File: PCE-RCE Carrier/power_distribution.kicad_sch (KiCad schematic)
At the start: 21 parts, among them J2 XT60PW-F, J3 XT60PW-F, J4 XT60PW-F, J8 Conn_01x02_Pin, U1 TPS75533KTTRG3, U2 TPS54302DDCR, U3 BD6222HFP-TR

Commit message: stoning my cap
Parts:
- removed CR1: SDM40E20LC-7, SOT-23_DIO, symbol SDM40E20LC_7:SDM40E20LC-7
- added D1: RB496EATR, DIO_FTZ_ROM, symbol RB496EATR:RB496EATR
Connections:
- net VBAT1: now also D1.1
- net VBAT2: now also D1.3
- net at J4.1: now also D1.4, D1.5
- no-connect marks 1 -> 2
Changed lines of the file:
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@@
+	)
+	(junction
+		(at 86.36 81.28)
+		(diameter 0)
+		(color 0 0 0 0)
 	)
 	(junction
@@
 	)
 	(no_connect
+		(at 55.88 86.36)
+	)
+	(no_connect
 		(at 93.98 88.9)
 	)
@@
 	(wire
 		(pts
+			(xy 52.07 91.44) (xy 55.88 91.44)
+		)
+		(stroke
+			(width 0)
+			(type default)
+		)
+	)
+	(wire
+		(pts
 			(xy 96.52 50.8) (xy 96.52 49.53)
 		)
@@
 	(wire
 		(pts
+			(xy 52.07 83.82) (xy 52.07 91.44)
+		)
+		(stroke
+			(width 0)
+			(type default)
+		)
+	)
+	(wire
+		(pts
 			(xy 92.71 170.18) (xy 92.71 172.72)
 		)
@@
 	(wire
 		(pts
-			(xy 92.71 81.28) (xy 93.98 81.28)
+			(xy 86.36 81.28) (xy 93.98 81.28)
 		)
 		(stroke
@@
 	(wire
 		(pts
+			(xy 86.36 81.28) (xy 86.36 91.44)
+		)
+		(stroke
+			(width 0)
+			(type default)
+		)
+	)
+	(wire
+		(pts
 			(xy 22.86 151.13) (xy 22.86 147.32)
 		)
@@
 	(wire
 		(pts
-			(xy 50.8 81.28) (xy 52.07 81.28)
+			(xy 50.8 81.28) (xy 55.88 81.28)
 		)
 		(stroke
@@
 	)
 	(symbol
-		(lib_id "SDM40E20LC_7:SDM40E20LC-7")
-		(at 52.07 81.28 0)
-		(unit 1)
-		(body_style 1)
-		(exclude_from_sim no)
-		(in_bom yes)
-		(on_board yes)
-		(in_pos_files yes)
-		(dnp no)
-		(fields_autoplaced yes)
-		(property "Reference" "CR1"
-			(at 72.39 71.12 0)
-			(show_name no)
-			(do_not_autoplace no)
-			(effects
-				(font
-					(size 1.524 1.524)
-				)
-			)
-		)
-		(property "Value" "SDM40E20LC-7"
-			(at 72.39 73.66 0)
-			(show_name no)
-			(do_not_autoplace no)
-			(effects
-				(font
-					(size 1.524 1.524)
-				)
-			)
-		)
-		(property "Footprint" "SOT-23_DIO"
-			(at 52.07 81.28 0)
-			(hide yes)
-			(show_name no)
-			(do_not_autoplace no)
-			(effects
-				(font
-					(size 1.27 1.27)
-					(italic yes)
-				)
-			)
-		)
-		(property "Datasheet" "SDM40E20LC-7"
-			(at 52.07 81.28 0)
-			(hide yes)
-			(show_name no)
-			(do_not_autoplace no)
-			(effects
-				(font
-					(size 1.27 1.27)
-					(italic yes)
-				)
-			)
-		)
-		(property "Description" ""
-			(at 52.07 81.28 0)
-			(hide yes)
-			(show_name no)
-			(do_not_autoplace no)
-			(effects
-				(font
-					(size 1.27 1.27)
-				)
-			)
-		)
-		(pin "3"
-		)
-		(pin "1"
-		)
-		(pin "2"
-		)
-		(instances
-			(project "PCE-RCE Carrier"
-				(path "/061bd5f9-7321-49d7-bd52-d55a9dc51a00/b13c5c10-72c7-47f9-aac2-179cc68eb567"
-					(reference "CR1")
-					(unit 1)
-				)
-			)
-		)
-	)
-	(symbol
 		(lib_id "power:GND")
 		(at 101.6 180.34 0)
@@
 					(unit 1)
 				)
+			)
+		)
+	)
+	(symbol
+		(lib_id "RB496EATR:RB496EATR")
+		(at 55.88 81.28 0)
+		(unit 1)
+		(body_style 1)
+		(exclude_from_sim no)
+		(in_bom yes)
+		(on_board yes)
+		(in_pos_files yes)
+		(dnp no)
+		(fields_autoplaced yes)
+		(property "Reference" "D1"
+			(at 71.12 73.66 0)
+			(show_name no)
+			(do_not_autoplace no)
+			(effects
+				(font
+					(size 1.524 1.524)
+				)
+			)
+		)
+		(property "Value" "RB496EATR"
+			(at 71.12 76.2 0)
+			(show_name no)
+			(do_not_autoplace no)
+			(effects
+				(font
+					(size 1.524 1.524)
+				)
+			)
+		)
+		(property "Footprint" "DIO_FTZ_ROM"
+			(at 55.88 81.28 0)
+			(hide yes)
+			(show_name no)
+			(do_not_autoplace no)
+			(effects
+				(font
+					(size 1.27 1.27)
+					(italic yes)
+				)
+			)
+		)
+		(property "Datasheet" "RB496EATR"
+			(at 55.88 81.28 0)
+			(hide yes)
+			(show_name no)
+			(do_not_autoplace no)
+			(effects
+				(font
+					(size 1.27 1.27)
+					(italic yes)
+				)
+			)
+		)
+		(property "Description" ""
+			(at 55.88 81.28 0)
+			(hide yes)
+			(show_name no)
+			(do_not_autoplace no)
+			(effects
+				(font
+					(size 1.27 1.27)
+				)
+			)
+		)
+		(pin "5"
+		)
+		(pin "2"
+		)
+		(pin "1"
+		)
+		(pin "3"
+		)
+		(pin "4"
+		)
+		(instances
+			(project "PCE-RCE Carrier"
+				(path "/061bd5f9-7321-49d7-bd52-d55a9dc51a00/b13c5c10-72c7-47f9-aac2-179cc68eb567"
+					(reference "D1")
+					(unit 1)
+				)

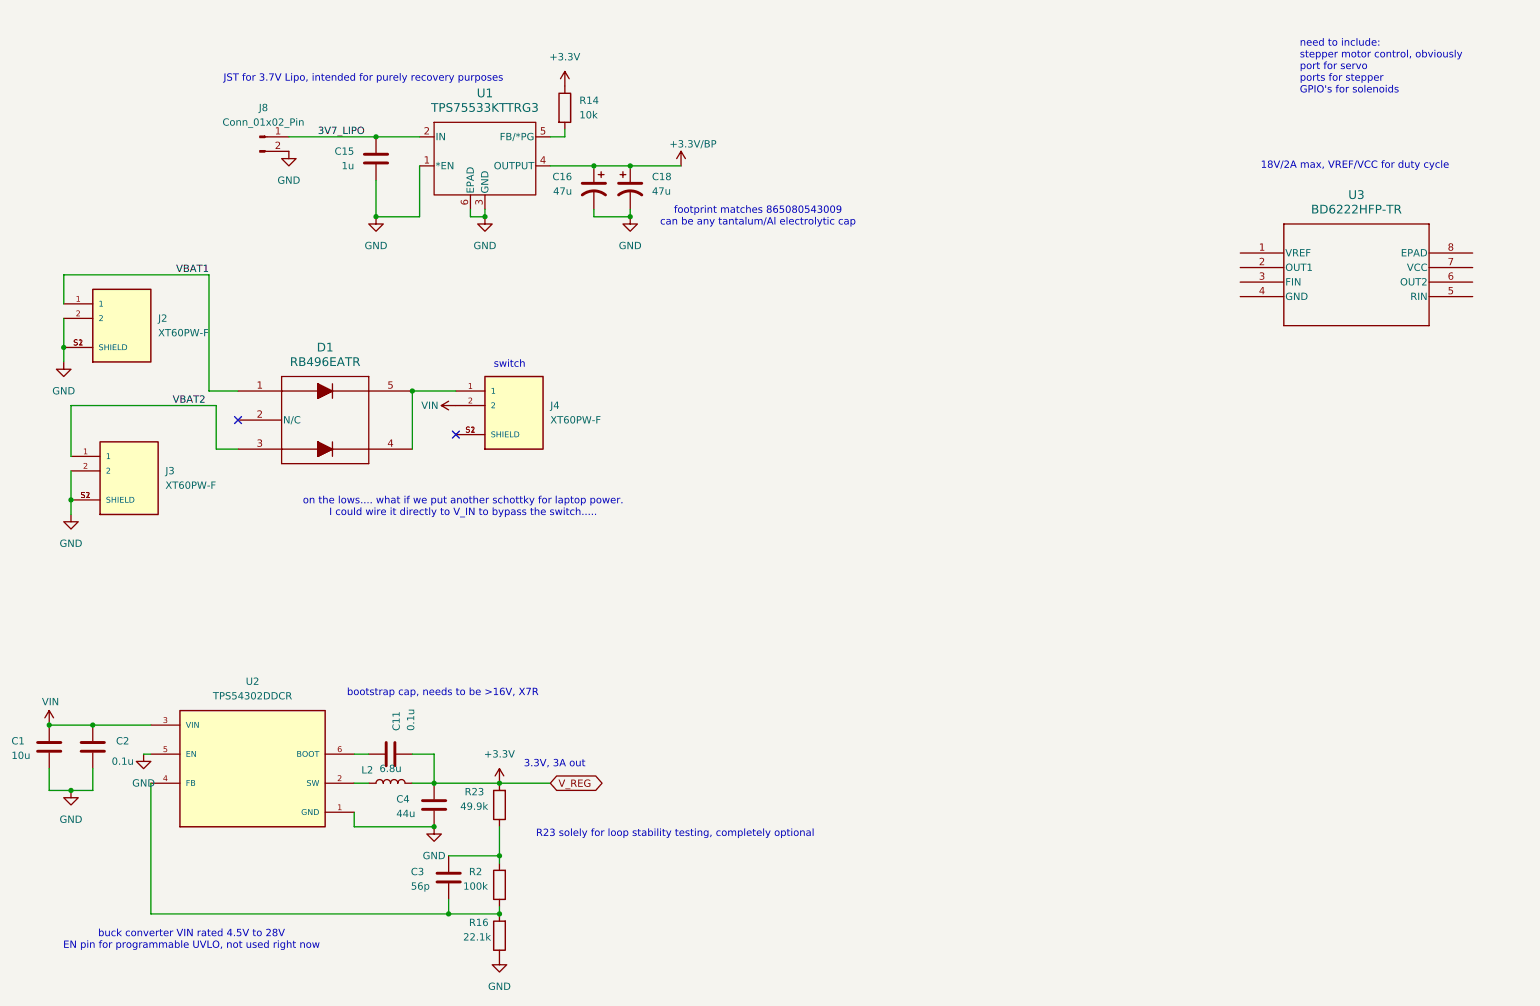
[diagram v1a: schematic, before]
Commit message: H-Bridge wiring + motor ports, cleaned up carrier schematics, added MISO source terminating resistors on carriers
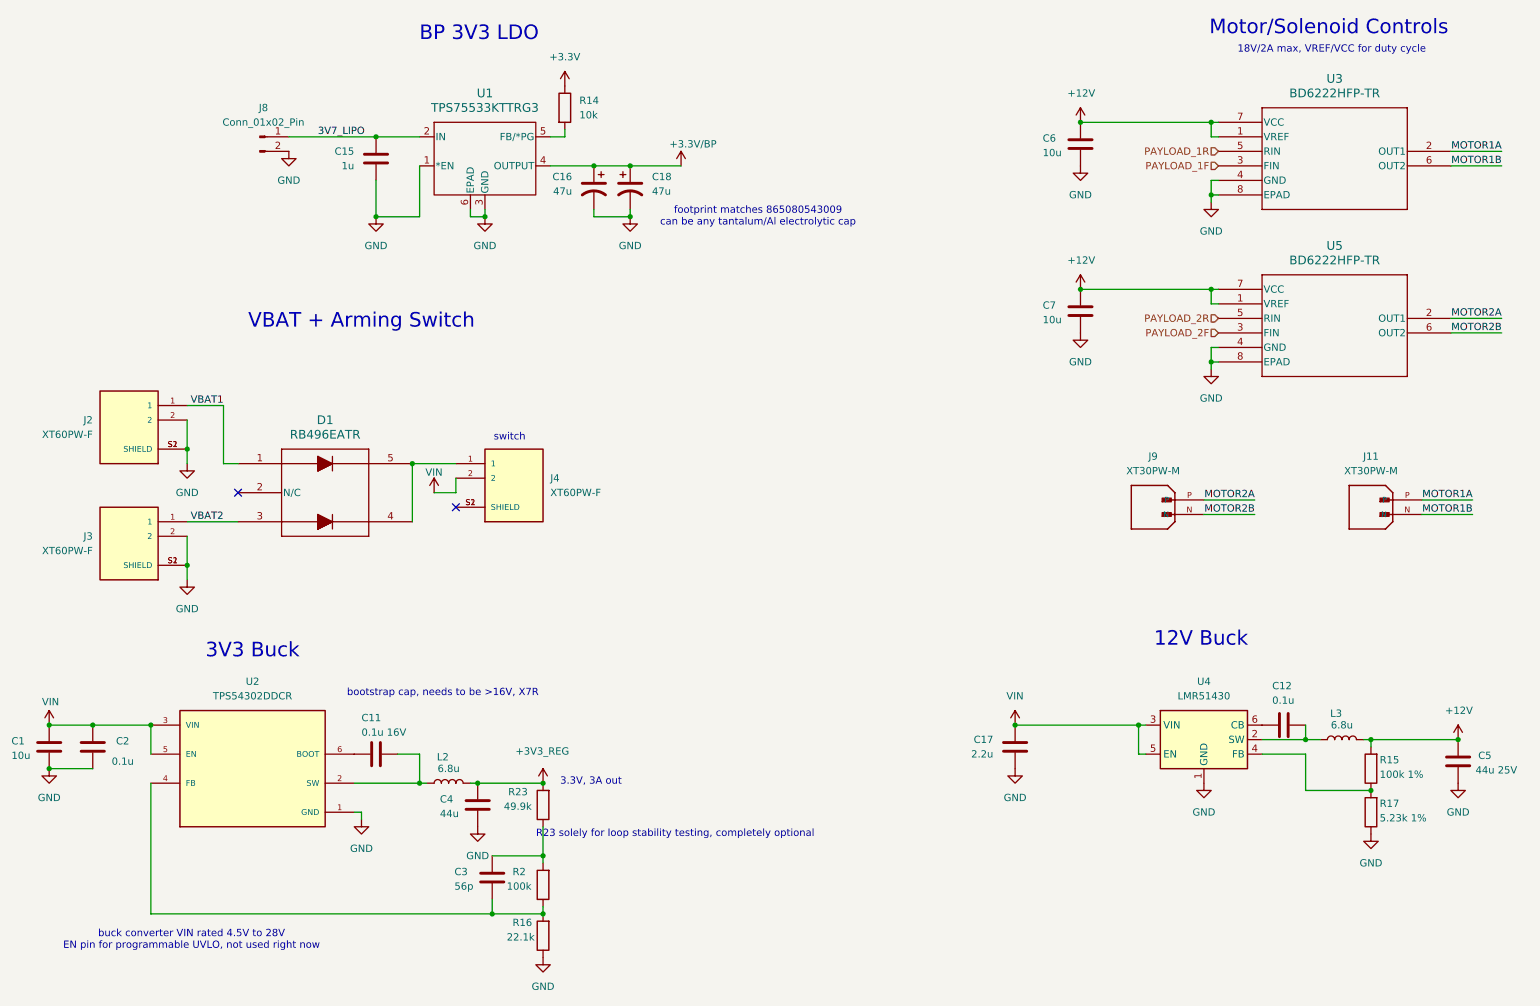
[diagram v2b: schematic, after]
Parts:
- added C12: 0.1u, Capacitor_SMD:C_0805_2012Metric, symbol Device:C
- added C17: 2.2u, Capacitor_SMD:C_0805_2012Metric, symbol Device:C
- added C5: 44u 25V, Capacitor_SMD:C_0805_2012Metric, symbol Device:C
- added C6, C7: 10u, Capacitor_SMD:C_0805_2012Metric, symbol Device:C
- added J11, J9: XT30PW-M, XT30PW-M:AMASS_XT30PW-M, symbol XT30PW-M:XT30PW-M
- added L3: 6.8u, Inductor_SMD:L_1008_2520Metric, symbol Device:L
- added R15: 100k 1%, Resistor_SMD:R_0603_1608Metric, symbol Device:R
- added R17: 5.23k 1%, Resistor_SMD:R_0603_1608Metric, symbol Device:R
- added U4: LMR51430, Package_TO_SOT_SMD:SOT-23-6, symbol Regulator_Switching:LMR51430
- added U5: BD6222HFP-TR, HRP7_ROM, symbol BD6222HFP-TR:BD6222HFP-TR
- C11: value 0.1u -> 0.1u 16V
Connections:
- net +3.3V: no longer C11.2, C4.1, L2.2, R23.2
- net GND: now also U3.4 (GND), U3.8 (EPAD), C17.2, C5.2, C6.2, C7.2, R17.1, U4.1 (GND), U5.4 (GND), U5.8 (EPAD); no longer U2.5 (EN)
- net VIN: now also U2.5 (EN), C17.1, U4.3 (VIN), U4.5 (EN)
- net at L2.1, U2.2 (SW): now also C11.2
- net +12V: now reaches U3.1 (VREF)
- net +12V: now also U3.7 (VCC), C5.1, C6.1, C7.1, L3.2, R15.2, U5.1 (VREF), U5.7 (VCC)
- net MOTOR1A: now reaches U3.2 (OUT1)
- net MOTOR1A: now also J11.P
- net PAYLOAD_1F: now reaches U3.3 (FIN)
- net PAYLOAD_1R: now reaches U3.5 (RIN)
- net MOTOR1B: now reaches U3.6 (OUT2)
- net MOTOR1B: now also J11.N
- new net: C12.1, U4.6 (CB)
- new net: C12.2, L3.1, U4.2 (SW)
- new net: R15.1, R17.2, U4.4 (FB)
- new net +3V3_REG: C4.1, L2.2, R23.2
- new net MOTOR2A: J9.P, U5.2 (OUT1)
- new net MOTOR2B: J9.N, U5.6 (OUT2)
- new net PAYLOAD_2F: U5.3 (FIN)
- new net PAYLOAD_2R: U5.5 (RIN)
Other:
- note added: "12V Buck"
- note added: "3V3 Buck"
- note added: "BP 3V3 LDO"
- note added: "Motor/Solenoid Controls"
- note added: "VBAT + Arming Switch"
- note removed: "JST for 3.7V Lipo, intended for purely recovery purposes"
- note removed: "need to include: stepper motor control, obviously port for servo ports for stepper GPIO's for solenoids"
- note removed: "on the lows.... what if we put another schottky for laptop power. I could wire it directly to V_IN to bypass the switch....."
- moved on the sheet: C11, C3, D1, J2, J3, J4, R16, R2, R23

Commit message: carrier board comments
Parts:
- removed D1: RB496EATR, DIO_FTZ_ROM, symbol RB496EATR:RB496EATR
- removed J3: XT60PW-F, XT60PW-F:AMASS_XT60PW-F, symbol XT60PW-F:XT60PW-F
- R23: value 49.9k -> 49.9
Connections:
- net VBAT1 is gone; now on net VBAT: J2.1
- net VBAT: now reaches J4.1
- no-connect marks 2 -> 1
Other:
- moved on the sheet: J2, J4

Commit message: mfw high power components are large
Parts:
- removed J11, J9: XT30PW-M, XT30PW-M:AMASS_XT30PW-M, symbol XT30PW-M:XT30PW-M
- added J3, J9: XT30UPB-M, XT30UPB-M:AMASS_XT30UPB-M, symbol XT30UPB-M:XT30UPB-M
- J8: footprint (none) -> Connector_JST:JST_PH_B2B-PH-K_1x02_P2.00mm_Vertical
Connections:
- net MOTOR1A: now also J9.P
- net MOTOR1B: now also J9.N
- net MOTOR2A: now also J3.P
- net MOTOR2B: now also J3.N

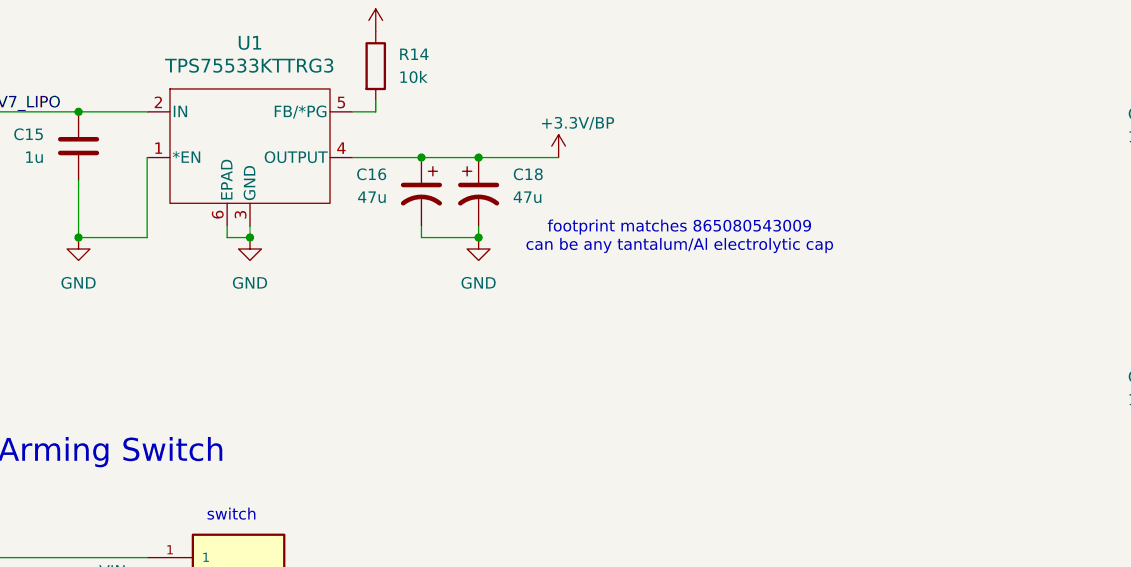
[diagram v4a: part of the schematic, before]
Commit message: some pce routing, switched out ace battery connectors for vertical xt30
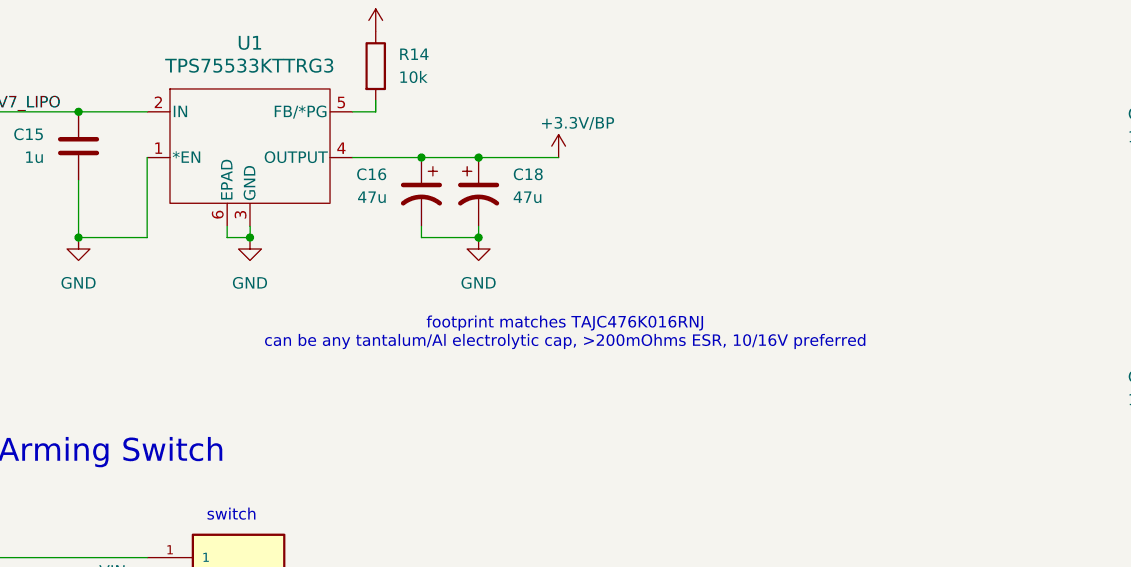
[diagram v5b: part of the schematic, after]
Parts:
- C16, C18: footprint Capacitor_SMD:CP_Elec_6.3x5.4 -> Capacitor_Tantalum_SMD:CP_EIA-6032-28_Kemet-C
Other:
- note added: "footprint matches TAJC476K016RNJ can be any tantalum/Al electrolytic cap, >200mOhms ESR, 10/16V preferred"
- note removed: "footprint matches 865080543009 can be any tantalum/Al electrolytic cap"
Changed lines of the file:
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@@
 		(comment 1 "Department of Electrical and Systems Engineering")
 	)
-	(text "footprint matches 865080543009\ncan be any tantalum/Al electrolytic cap"
+	(text "footprint matches TAJC476K016RNJ\ncan be any tantalum/Al electrolytic cap, >200mOhms ESR, 10/16V preferred\n"
 		(exclude_from_sim no)
-		(at 146.812 50.8 0)
+		(at 134.112 61.468 0)
 		(effects
 			(font
@@
 			)
 		)
-		(property "Footprint" "Capacitor_SMD:CP_Elec_6.3x5.4"
+		(property "Footprint" "Capacitor_Tantalum_SMD:CP_EIA-6032-28_Kemet-C"
 			(at 118.11 45.72 0)
 			(hide yes)
@@
 			)
 		)
-		(property "Footprint" "Capacitor_SMD:CP_Elec_6.3x5.4"
+		(property "Footprint" "Capacitor_Tantalum_SMD:CP_EIA-6032-28_Kemet-C"
 			(at 124.46 45.72 0)
 			(hide yes)

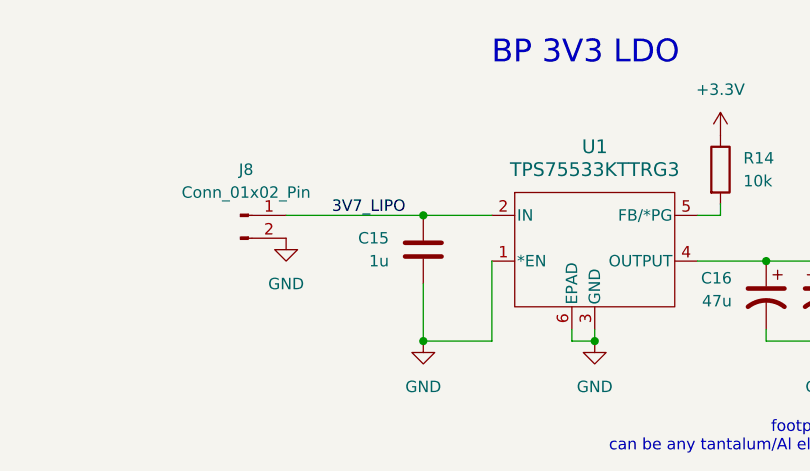
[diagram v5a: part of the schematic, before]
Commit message: updated pyro circuit to be like easymini, lowk will prob make it a separate carrier
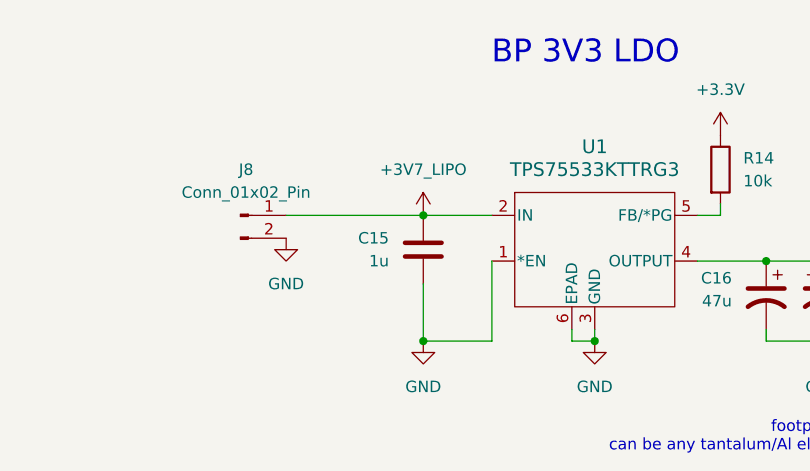
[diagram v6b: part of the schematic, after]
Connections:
- net 3V7_LIPO renamed +3V7_LIPO
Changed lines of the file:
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@@
 		)
 	)
-	(label "3V7_LIPO"
-		(at 69.85 36.83 0)
-		(effects
-			(font
-				(size 1.27 1.27)
-			)
-			(justify left bottom)
-		)
-	)
 	(label "MOTOR2A"
 		(at 276.86 68.58 180)
@@
 					(unit 1)
 				)
+			)
+		)
+	)
+	(symbol
+		(lib_id "power:+3.3V")
+		(at 80.01 36.83 0)
+		(unit 1)
+		(body_style 1)
+		(exclude_from_sim no)
+		(in_bom yes)
+		(on_board yes)
+		(in_pos_files yes)
+		(dnp no)
+		(fields_autoplaced yes)
+		(property "Reference" "#PWR083"
+			(at 80.01 40.64 0)
+			(hide yes)
+			(show_name no)
+			(do_not_autoplace no)
+			(effects
+				(font
+					(size 1.27 1.27)
+				)
+			)
+		)
+		(property "Value" "+3V7_LIPO"
+			(at 80.01 31.75 0)
+			(show_name no)
+			(do_not_autoplace no)
+			(effects
+				(font
+					(size 1.27 1.27)
+				)
+			)
+		)
+		(property "Footprint" ""
+			(at 80.01 36.83 0)
+			(hide yes)
+			(show_name no)
+			(do_not_autoplace no)
+			(effects
+				(font
+					(size 1.27 1.27)
+				)
+			)
+		)
+		(property "Datasheet" ""
+			(at 80.01 36.83 0)
+			(hide yes)
+			(show_name no)
+			(do_not_autoplace no)
+			(effects
+				(font
+					(size 1.27 1.27)
+				)
+			)
+		)
+		(property "Description" "Power symbol creates a global label with name \"+3.3V\""
+			(at 80.01 36.83 0)
+			(hide yes)
+			(show_name no)
+			(do_not_autoplace no)
+			(effects
+				(font
+					(size 1.27 1.27)
+				)
+			)
+		)
+		(pin "1"
+		)
+		(instances
+			(project "PCE-RCE Carrier"
+				(path "/061bd5f9-7321-49d7-bd52-d55a9dc51a00/b13c5c10-72c7-47f9-aac2-179cc68eb567"
+					(reference "#PWR083")
+					(unit 1)
+				)
